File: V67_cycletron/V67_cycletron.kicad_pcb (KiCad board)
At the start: 2 copper layers, 99 x 101 mm, 41 parts, among them J1 USB_C_Receptacle_USB2.0_16P, J2 Screw_Terminal_01x02, J3 Screw_Terminal_01x14, J4 Screw_Terminal_01x02, U1 ESP32-S3-WROOM-1, U2 LM1117DT-3.3, U3 LM1117DT-5.0

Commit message: test commit, added schotsky diode
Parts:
- removed D1: 1N4001, Diode_THT:D_DO-41_SOD81_P10.16mm_Horizontal
- added D3: D_Schottky, Diode_SMD:D_SMA, F.Cu at (188.5, 33.5)
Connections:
- J2 pad 1: +12V -> Net-(D3-A)
- U3 pad 3: Net-(D1-K) -> +12V
- reg_5V_smoothing_caps_in1 pad 1: Net-(D1-K) -> +12V
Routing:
- net +12V: track 0.00 -> 20.1 mm
- net Net-(D1-K): track 17.9 -> 0.00 mm
- net Net-(D3-A): track 0.00 -> 8.00 mm

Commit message: got all parts to sync to jlcpcb
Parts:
- removed Trans_3: 5023520200, Connector_4:CONN_SD-502352-001_02_MOL
- added mosfet3: 5023520200, Connector_4:CONN_SD-502352-001_02_MOL, F.Cu at (193.5, 114.8)
- 3v3in1: renamed from reg_3v3_smoother_in1; footprint Capacitor_THT:CP_Radial_D6.3mm_P2.50mm -> Capacitor_SMD:CP_Elec_6.3x5.4
- 3v3out1: renamed from reg_3v3_smoother_out1; footprint Capacitor_THT:CP_Radial_D5.0mm_P2.50mm -> Capacitor_SMD:CP_Elec_4x5.4
- 5Vin1: renamed from reg_5V_smoothing_caps_in1; footprint Capacitor_THT:CP_Radial_D6.3mm_P2.50mm -> Capacitor_SMD:CP_Elec_6.3x5.4
- 5Vout1: renamed from reg_5V_smoothing_caps_out1; footprint Capacitor_THT:CP_Radial_D5.0mm_P2.50mm -> Capacitor_SMD:CP_Elec_4x5.4
- motorc1: renamed from motor1_c1; value C_Polarized -> 100uF; footprint Capacitor_THT:CP_Radial_D6.3mm_P2.50mm -> Capacitor_SMD:CP_Elec_6.3x5.4
- motorc2: renamed from motor2_c1; value C_Polarized -> 100uF; footprint Capacitor_THT:CP_Radial_D6.3mm_P2.50mm -> Capacitor_SMD:CP_Elec_6.3x5.4
- moved motorc2 4.11 mm to (196.8, 38.6)
- moved 3v3in1 2.97 mm to (145.8, 33.8)
- moved motorc1 2.28 mm to (184.9, 78.7)
- moved Motor_1 1.85 mm to (159.3, 86.3)
- moved 5Vout1 1.81 mm to (166.9, 26.0)
- moved Motor2 1.80 mm to (195.3, 69.5)
- moved Motor1 1.58 mm to (195.6, 85.0)
- renumbered C6 to C1, C8 to C2, D3 to D1, J3 to IO1, R4 to R1, R3 to R2, R1 to R_En1, R2 to R_boot1, U3 to U1, U1 to U3, J2 to input1, Trans_1 to mosfet1, Trans_2 to mosfet2, mosfet1 to mosfet4, mosfet2 to mosfet5, mosfet3 to mosfet6, J4 to power1, esp_smoothingcaps_1 to smooth_cap1, esp_smoothingcaps_2 to smooth_cap2, tr3 to tr1, tr1 to tr3, VoltageDivider1 to vd1, vd_c4 to vd_c1, vd_c3 to vd_c2
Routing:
- net 3V3: track 81.4 -> 70.1 mm
- net Motor1_B1: track 28.7 -> 32.4 mm
- net Motor1_A2: track 37.8 -> 41.1 mm
- net Motor1_FLT: track 19.7 -> 17.1 mm
- net +12V: track 20.1 -> 18.1 mm
- net Motor1_STEP: track 12.4 -> 10.6 mm
- net Motor1_M2: track 20.2 -> 18.4 mm
- net Motor1_M1: track 23.3 -> 21.4 mm
- net Motor1_M0: track 26.4 -> 24.5 mm
- net Motor1_DIR: track 9.51 -> 7.66 mm
- net Motor1_A1: track 23.7 -> 25.5 mm
- net Motor1_EN: track 31.7 -> 29.9 mm
- net Motor1_B2: track 19.0 -> 20.8 mm
- net GND: vias 16 -> 23
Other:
- board size 99 x 101 mm -> 102 x 101 mm

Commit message: moved IO
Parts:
- added ?: , , F.Cu at (105.2, 23.4)
- added ?: , , F.Cu at (200.7, 23.4)
- added ?: , , F.Cu at (105.2, 120.9)
- added ?: , , F.Cu at (200.7, 120.9)
- moved IO1 6.25 mm to (109.2, 111.9)
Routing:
- net I19: track 53.2 -> 46.2 mm
- net I18: track 48.5 -> 42.4 mm
- net 3V3: track 70.1 -> 74.7 mm
- net I09: track 29.7 -> 25.6 mm
- net I15: track 35.3 -> 31.5 mm
- net I11: track 32.0 -> 28.2 mm
- net I10: track 30.6 -> 26.9 mm
- net I17: track 43.0 -> 39.2 mm
- net I16: track 39.2 -> 35.4 mm
- net I12: track 33.0 -> 29.3 mm
- net IO4: track 35.2 -> 37.9 mm
- net IO6: track 28.9 -> 30.7 mm
- net I08: track 28.7 -> 27.2 mm
- net IO5: track 32.5 -> 34.1 mm
- net IO7: track 27.4 -> 28.7 mm
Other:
- board size 102 x 101 mm -> 102.1 x 103 mm

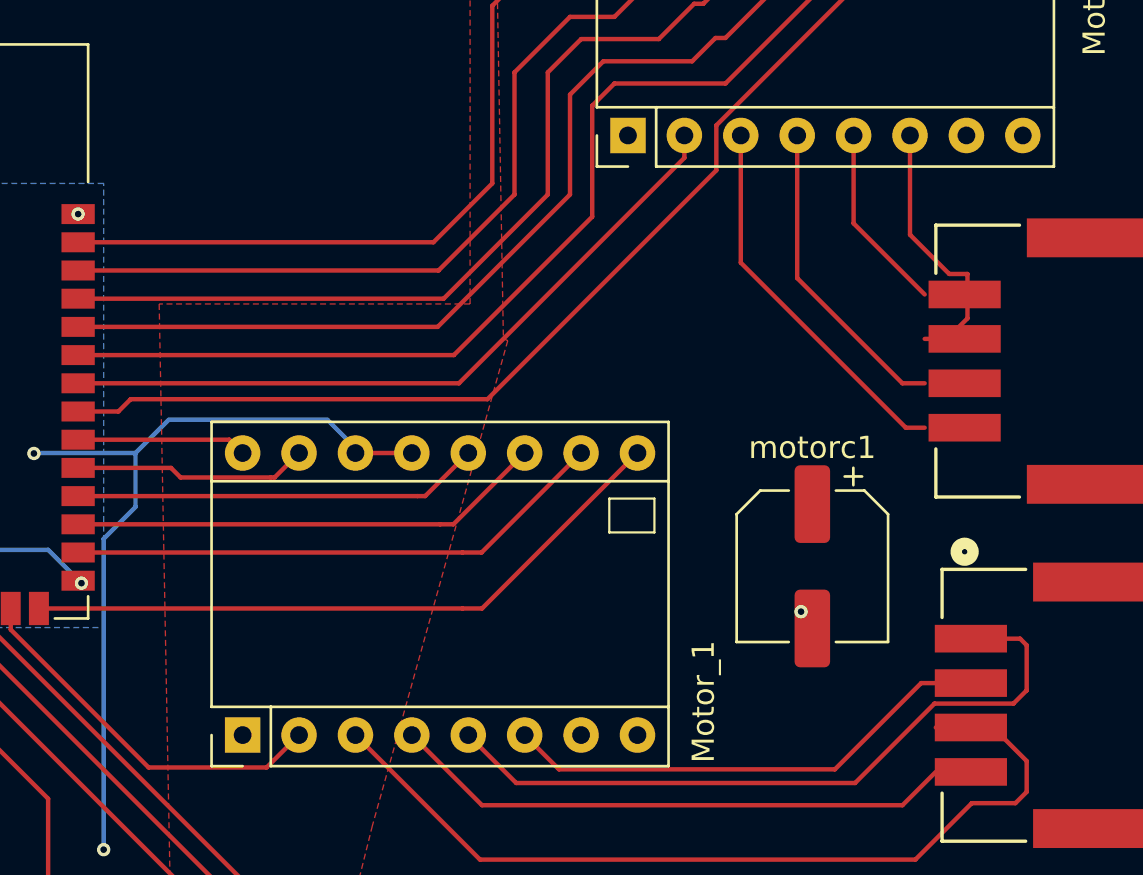
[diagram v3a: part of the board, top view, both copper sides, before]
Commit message: fixed some issues with vias and motor connector placement
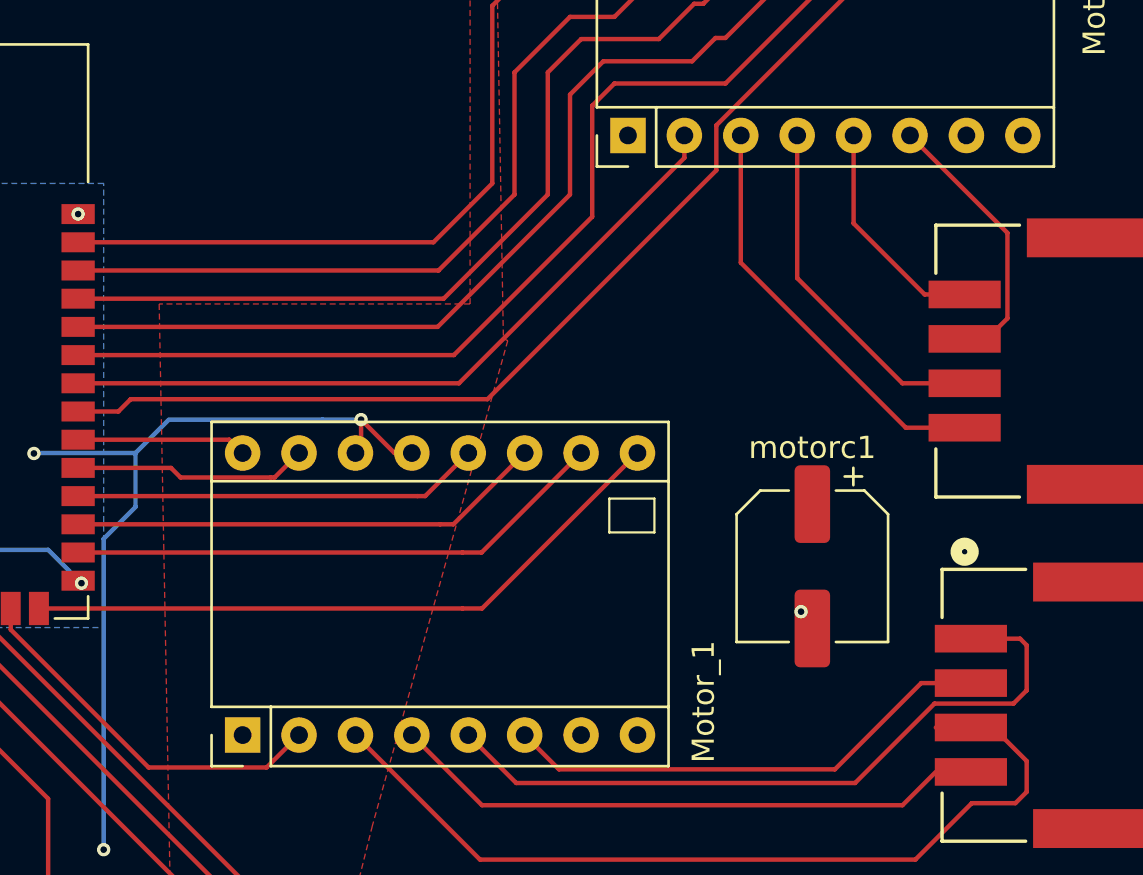
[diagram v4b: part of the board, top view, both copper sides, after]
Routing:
- net Motor2_A1: track 14.1 -> 16.7 mm
- net Motor2_B1: track 8.49 -> 10.3 mm
- net Motor2_A2: track 17.1 -> 18.9 mm
- net 3V3: track 74.7 -> 76.2 mm
- net GND: vias 23 -> 22
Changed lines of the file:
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@@
-	)
-	(via
-		(at 174.498 86.34)
-		(size 0.6)
-		(drill 0.3)
-		(layers "F.Cu" "B.Cu")
-		(net 1)
 	)
 	(via
@@
 	)
 	(segment
+		(start 189.121098 72.499999)
+		(end 191.7708 72.499999)
+		(width 0.2)
+		(layer "F.Cu")
+		(net 29)
+	)
+	(segment
 		(start 181.69 59.34)
 		(end 181.69 65.068901)
@@
 	)
 	(segment
-		(start 189.121098 72.499999)
-		(end 189.971 72.499999)
-		(width 0.2)
-		(layer "F.Cu")
-		(net 29)
-	)
-	(segment
-		(start 191.076701 65.576701)
-		(end 191.8976 65.576701)
+		(start 193.6974 63.7274)
+		(end 193.6974 67.576699)
 		(width 0.2)
 		(layer "F.Cu")
@@
 	)
 	(segment
+		(start 193.6974 67.576699)
+		(end 192.7741 68.499999)
+		(width 0.2)
+		(layer "F.Cu")
+		(net 30)
+	)
+	(segment
+		(start 192.7741 68.499999)
+		(end 191.7708 68.499999)
+		(width 0.2)
+		(layer "F.Cu")
+		(net 30)
+	)
+	(segment
 		(start 189.31 59.34)
-		(end 189.31 63.81)
-		(width 0.2)
-		(layer "F.Cu")
-		(net 30)
-	)
-	(segment
-		(start 191.8976 65.576701)
-		(end 191.8976 67.576699)
-		(width 0.2)
-		(layer "F.Cu")
-		(net 30)
-	)
-	(segment
-		(start 189.31 63.81)
-		(end 191.076701 65.576701)
-		(width 0.2)
-		(layer "F.Cu")
-		(net 30)
-	)
-	(segment
-		(start 191.8976 67.576699)
-		(end 190.9743 68.499999)
-		(width 0.2)
-		(layer "F.Cu")
-		(net 30)
-	)
-	(segment
-		(start 190.9743 68.499999)
-		(end 189.971 68.499999)
+		(end 193.6974 63.7274)
 		(width 0.2)
 		(layer "F.Cu")
@@
 	)
 	(segment
+		(start 189.971 66.500001)
+		(end 191.7708 66.500001)
+		(width 0.2)
+		(layer "F.Cu")
+		(net 35)
+	)
+	(segment
 		(start 186.77 63.299001)
 		(end 189.971 66.500001)
@@
 	)
 	(segment
+		(start 188.9677 70.500001)
+		(end 191.7708 70.500001)
+		(width 0.2)
+		(layer "F.Cu")
+		(net 39)
+	)
+	(segment
+		(start 191.119999 70.500001)
+		(end 191.008 70.612)
+		(width 0.2)
+		(layer "F.Cu")
+		(net 39)
+	)
+	(segment
 		(start 184.23 59.34)
 		(end 184.23 65.762301)
@@
 	)
 	(segment
+		(start 191.7708 70.500001)
+		(end 191.119999 70.500001)
+		(width 0.2)
+		(layer "F.Cu")
+		(net 39)
+	)
+	(segment
 		(start 184.23 65.762301)
 		(end 188.9677 70.500001)
-		(width 0.2)
-		(layer "F.Cu")
-		(net 39)
-	)
-	(segment
-		(start 188.9677 70.500001)
-		(end 189.971 70.500001)
 		(width 0.2)
 		(layer "F.Cu")
@@
 	)
 	(segment
+		(start 164.592 73.386)
+		(end 164.338 73.64)
+		(width 0.2)
+		(layer "F.Cu")
+		(net 63)
+	)
+	(segment
 		(start 133.575 64.575)
 		(end 134 64.15)
@@
 	)
 	(segment
-		(start 164.338 73.64)
-		(end 166.878 73.64)
-		(width 0.2)
-		(layer "F.Cu")
-		(net 63)
-	)
-	(segment
 		(start 154.5 34.5)
 		(end 154.705113 34.705113)
+		(width 0.2)
+		(layer "F.Cu")
+		(net 63)
+	)
+	(segment
+		(start 166.096 73.64)
+		(end 166.878 73.64)
 		(width 0.2)
 		(layer "F.Cu")
@@
 	)
 	(segment
+		(start 164.592 72.136)
+		(end 164.592 73.386)
+		(width 0.2)
+		(layer "F.Cu")
+		(net 63)
+	)
+	(segment
 		(start 154 33.5)
 		(end 154.5 34)
@@
 	)
 	(segment
+		(start 164.592 72.136)
+		(end 166.096 73.64)
+		(width 0.2)
+		(layer "F.Cu")
+		(net 63)
+	)
+	(segment
 		(start 154 36.8)
 		(end 154 30.5)
@@
 	)
 	(via
-		(at 164.338 73.64)
-		(size 0.6)
-		(drill 0.3)
-		(layers "F.Cu" "B.Cu")
-		(net 63)
-	)
-	(via
 		(at 149.86 73.66)
 		(size 0.6)
@@
 	)
 	(via
+		(at 164.592 72.136)
+		(size 0.6)
+		(drill 0.3)
+		(layers "F.Cu" "B.Cu")
+		(net 63)
+	)
+	(via
 		(at 153 91.5)
 		(size 0.6)
@@
 	)
 	(segment
-		(start 154.432 73.64)
-		(end 155.93 72.142)
+		(start 155.93 72.142)
+		(end 154.432 73.64)
+		(width 0.2)
+		(layer "B.Cu")
+		(net 63)
+	)
+	(segment
+		(start 164.592 72.136)
+		(end 162.846 72.136)
 		(width 0.2)
 		(layer "B.Cu")
@@
 	)
 	(segment
+		(start 162.84 72.142)
+		(end 155.93 72.142)
+		(width 0.2)
+		(layer "B.Cu")
+		(net 63)
+	)
+	(segment
+		(start 162.846 72.136)
+		(end 162.84 72.142)
+		(width 0.2)
+		(layer "B.Cu")
+		(net 63)
+	)
+	(segment
 		(start 154.432 73.64)
 		(end 149.88 73.64)
@@
 		(width 0.2)
 		(layer "B.Cu")
-		(net 63)
-	)
-	(segment
-		(start 155.93 72.142)
-		(end 163.074 72.142)
-		(width 0.2)
-		(layer "B.Cu")
-		(net 63)
-	)
-	(segment
-		(start 164.338 73.406)
-		(end 164.338 73.64)
-		(width 0.2)
-		(layer "B.Cu")
-		(net 63)
-	)
-	(segment
-		(start 163.074 72.142)
-		(end 164.338 73.406)
-		(width 0.2)
-		(layer "B.Cu")

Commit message: changed some stuff
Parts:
- removed power1: Screw_Terminal_01x02, TerminalBlock:TerminalBlock_MaiXu_MX126-5.0-02P_1x02_P5.00mm
- removed vd1: 5023520400, Connector_4:CONN_SD-502352-001_04_MOL
- added IO2: 5023520200, Connector_4:CONN_SD-502352-001_02_MOL, F.Cu at (107.2, 38.1)
- added IO3: 5023520200, Connector_4:CONN_SD-502352-001_02_MOL, F.Cu at (107.2, 47.8)
- added IO4: 5023520200, Connector_4:CONN_SD-502352-001_02_MOL, F.Cu at (107.2, 57.4)
- added J3: Screw_Terminal_01x11, TerminalBlock:TerminalBlock_MaiXu_MX126-5.0-11P_1x11_P5.00mm, F.Cu at (106.7, 116.7)
- added power3: Screw_Terminal_01x02, TerminalBlock:TerminalBlock_MaiXu_MX126-5.0-02P_1x02_P5.00mm, F.Cu at (133.2, 122.9)
- added power5: Screw_Terminal_01x02, TerminalBlock:TerminalBlock_MaiXu_MX126-5.0-02P_1x02_P5.00mm, F.Cu at (156.5, 22.9)
- added voltage_divider_2con1: 5023520200, Connector_4:CONN_SD-502352-001_02_MOL, F.Cu at (148.8, 122.4)
- IO1: value Screw_Terminal_01x14 -> 5023520200; footprint TerminalBlock:TerminalBlock_MaiXu_MX126-5.0-14P_1x14_P5.00mm -> Connector_4:CONN_SD-502352-001_02_MOL
- vd_r1: footprint Resistor_SMD:R_0805_2012Metric_Pad1.20x1.40mm_HandSolder -> Resistor_THT:R_Axial_DIN0207_L6.3mm_D2.5mm_P7.62mm_Horizontal
- moved IO1 83.7 mm to (107.2, 28.2), turned to -90 degrees
- moved mosfet1 7.92 mm to (166.7, 122.9)
- moved mosfet2 7.92 mm to (180.2, 122.8)
- moved mosfet3 7.92 mm to (193.2, 122.7)
- moved ? 5.95 mm to (103.1, 126.5)
- moved R_En1 5.72 mm to (117.9, 31.5)
- moved ? 5.59 mm to (200.7, 126.5)
- moved En1 5.47 mm to (117.9, 25.9)
- moved vd_c1 5.21 mm to (144.3, 102.6)
- moved Boot1 4.27 mm to (124.0, 25.9)
- moved R_boot1 4.27 mm to (124.0, 32.0)
- moved vd_c2 3.36 mm to (147.8, 100.1)
- moved ? 2.87 mm to (103.1, 21.3)
- moved mosfet4 2.71 mm to (167.1, 107.5)
- moved mosfet5 2.71 mm to (174.6, 107.5)
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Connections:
- IO1 pad 1: I19 -> IO4
- IO1 pad 2: I18 -> GND
- U3 pad 20: Therm- -> I20
- U3 pad 21: PWM -> Therm-
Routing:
- net I20: track 0.00 -> 53.3 mm
- net PWM: track 34.1 -> 0.00 mm
- net IO4: track 37.9 -> 59.8 mm
- net IO5: track 34.1 -> 49.7 mm
- net IO6: track 30.7 -> 41.7 mm
- net +5V: track 59.1 -> 68.9 mm
- net 3V3: track 76.2 -> 69.9 mm
- net mosfet2_o: track 7.12 -> 12.4 mm
- net mosfet1_o: track 8.49 -> 13.7 mm
- net Therm-: track 36.8 -> 41.7 mm
- net BOOT: track 68.1 -> 72.6 mm
- net IO7: track 28.7 -> 33.0 mm
- net mosfet3_o: track 10.3 -> 14.5 mm
- net En: track 54.4 -> 51.3 mm
- net I09: track 25.6 -> 28.2 mm
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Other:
- board size 102.1 x 103 mm -> 102.1 x 110.1 mm

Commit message: changed some stuff 2
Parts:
- added D2: D_Schottky, Diode_SMD:D_SMA, F.Cu at (178.8, 115.3)
- added D3: D_Schottky, Diode_SMD:D_SMA, F.Cu at (192.0, 114.8)
- added Dpower1: D_Schottky, Diode_SMD:D_SMA, F.Cu at (188.4, 33.5)
- input1: value Screw_Terminal_01x02 -> 5023520200; footprint TerminalBlock:TerminalBlock_MaiXu_MX126-5.0-02P_1x02_P5.00mm -> Connector_4:CONN_SD-502352-001_02_MOL
- moved D1 83.9 mm to (167.6, 114.8)
- moved input1 1.98 mm to (189.5, 23.8)
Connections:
- D1 pad 2: Net-(D1-A) -> mosfet1_o
- input1 pad 1: Net-(D1-A) -> Net-(Dpower1-A)
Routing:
- net GND: track 12.2 -> 22.6 mm, vias 21 -> 23
- net Net-(Dpower1-A): track 0.00 -> 8.00 mm
- net Net-(D1-A): track 8.00 -> 0.00 mm

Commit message: changed some stuff 3
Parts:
- moved 5Vin1 2.56 mm to (178.6, 25.5)
- moved input1 0.51 mm to (189.5, 24.3)
- moved power5 0.51 mm to (156.5, 23.4)
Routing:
- net GND: track 22.6 -> 12.2 mm, vias 23 -> 26
- net +5V: track 68.9 -> 64.6 mm
- net En: track 51.3 -> 53.8 mm
- net +12V: track 18.1 -> 19.7 mm, vias 0 -> 2

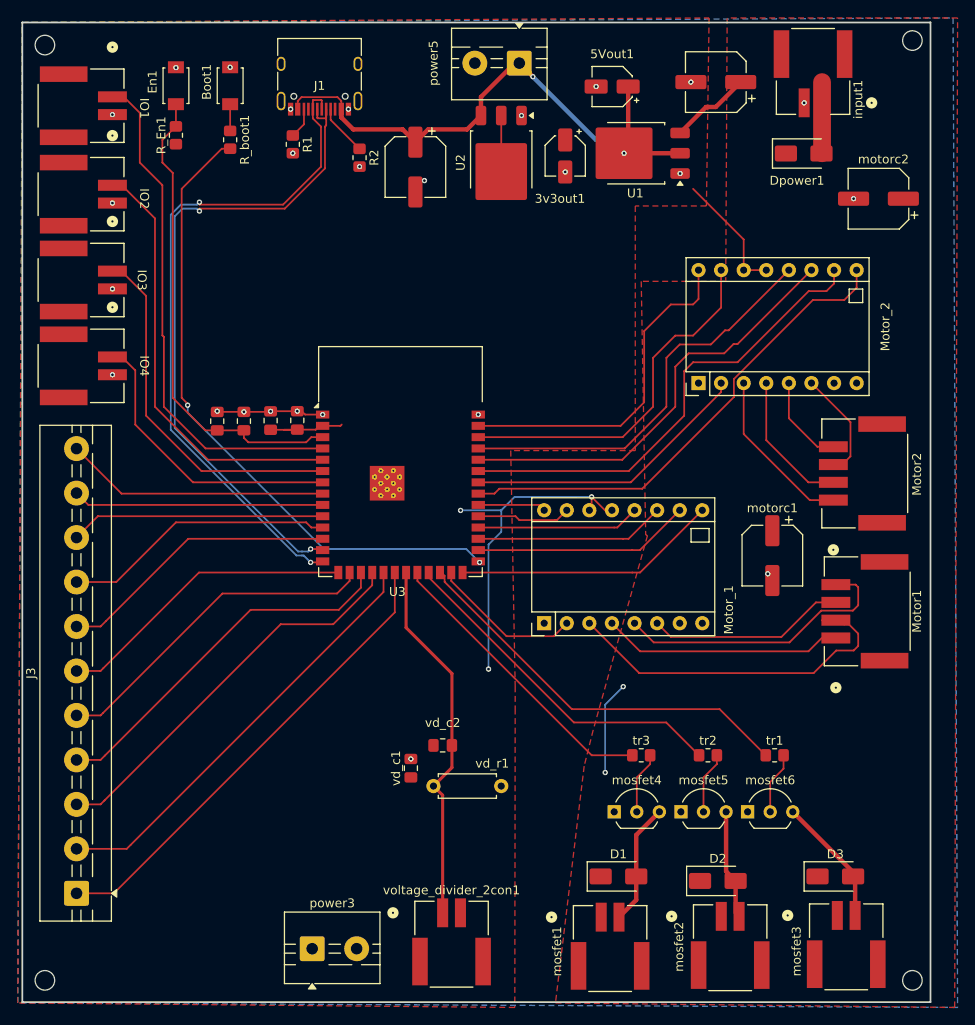
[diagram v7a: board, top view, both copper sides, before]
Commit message: changed mosfets added more terminals
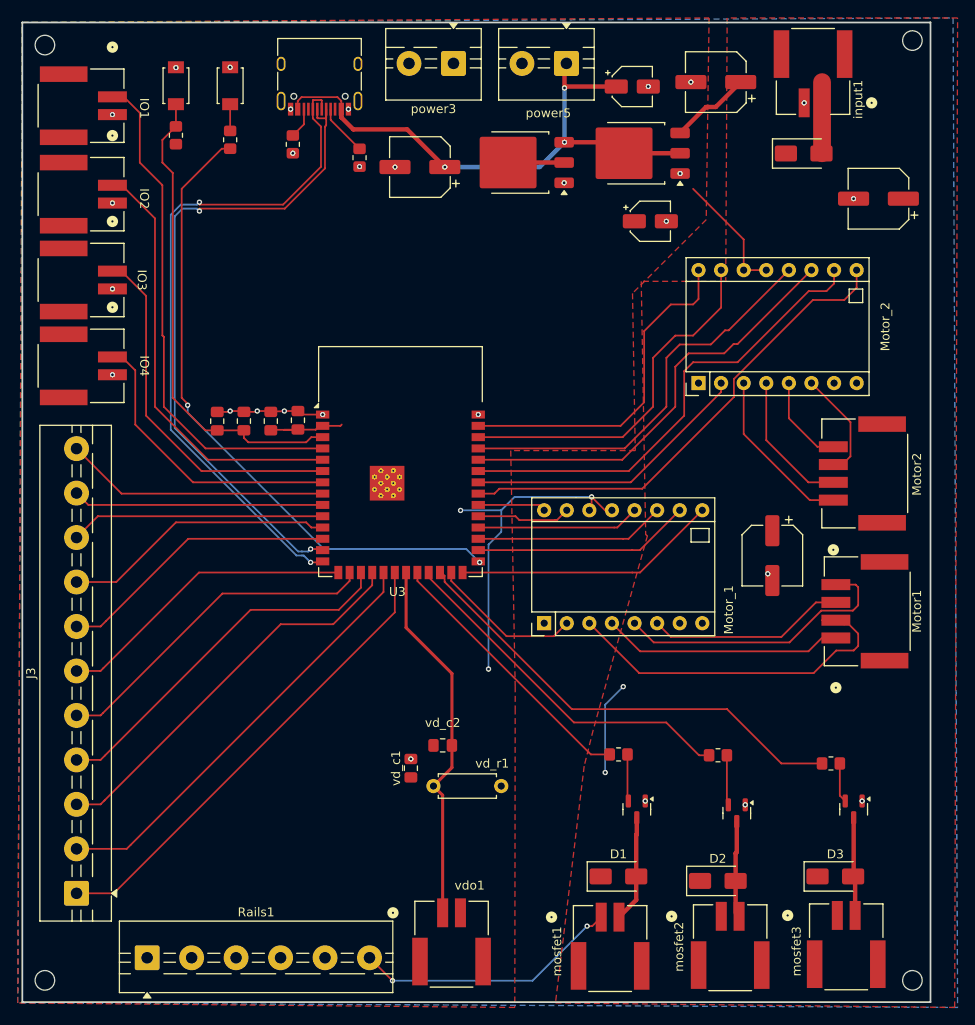
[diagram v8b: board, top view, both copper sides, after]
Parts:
- removed smooth_cap1: 100nF, Capacitor_SMD:C_0805_2012Metric_Pad1.18x1.45mm_HandSolder
- removed smooth_cap2: 22uF, Capacitor_SMD:C_0805_2012Metric_Pad1.18x1.45mm_HandSolder
- removed voltage_divider_2con1: 5023520200, Connector_4:CONN_SD-502352-001_02_MOL
- added Rails1: Screw_Terminal_01x06, TerminalBlock:TerminalBlock_MaiXu_MX126-5.0-06P_1x06_P5.00mm, F.Cu at (114.6, 124.0)
- added mccap1: 100nF, Capacitor_SMD:C_0805_2012Metric_Pad1.18x1.45mm_HandSolder, F.Cu at (131.6, 63.5)
- added mccap2: 22uF, Capacitor_SMD:C_0805_2012Metric_Pad1.18x1.45mm_HandSolder, F.Cu at (128.5, 63.6)
- added vdo1: 5023520200, Connector_4:CONN_SD-502352-001_02_MOL, F.Cu at (148.8, 122.4)
- mosfet4, mosfet5, mosfet6: value 2N7000 -> HD2305; footprint Package_TO_SOT_THT:TO-92_Inline_Wide -> Package_TO_SOT_SMD:SOT-23
- moved power3 100.8 mm to (149.1, 23.4), turned to 180 degrees
- moved 3v3out1 12.1 mm to (171.2, 41.1), turned to 0 degrees
- moved mosfet6 11.9 mm to (194.1, 107.3), turned to -90 degrees
- moved tr1 6.39 mm to (191.5, 102.1)
- moved mosfet5 6.28 mm to (180.9, 107.7), turned to -90 degrees
- moved power5 5.30 mm to (161.8, 23.4)
- moved mosfet4 2.56 mm to (169.7, 107.3), turned to -90 degrees
- moved tr3 2.55 mm to (167.6, 101.1)
- moved 5Vout1 2.26 mm to (169.2, 26.0), turned to 0 degrees
- moved U2 2.05 mm to (156.5, 34.5), turned to 180 degrees
- moved tr2 1.13 mm to (178.8, 101.2)
- moved 3v3in1 0.51 mm to (145.3, 35.1), turned to 180 degrees
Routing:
- net +12V: track 19.7 -> 49.8 mm, vias 2 -> 4
- net mosfet3_i: track 45.5 -> 52.2 mm
- net mosfet3_o: track 14.5 -> 11.5 mm
- net GND: track 12.2 -> 14.8 mm, vias 26 -> 28
- net mosfet1_i: track 33.2 -> 30.6 mm
- net Net-(mosfet6-G): track 6.98 -> 4.47 mm
- net mosfet1_o: track 13.7 -> 12.0 mm
- net Net-(mosfet4-G): track 6.98 -> 5.28 mm
- net mosfet2_o: track 12.4 -> 10.9 mm
- net Net-(mosfet5-G): track 6.98 -> 5.64 mm
- net mosfet2_i: track 39.2 -> 40.3 mm
- net +5V: track 64.6 -> 65.6 mm, vias 2 -> 3
